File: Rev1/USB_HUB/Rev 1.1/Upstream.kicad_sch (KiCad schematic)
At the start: 17 parts, among them IC1 TLV76733DGNR, IC2 TLV76733DGNR, J4 F3311A7H121014E200, U7 USBLC6-2SC6, U8 USBLC6-2SC6

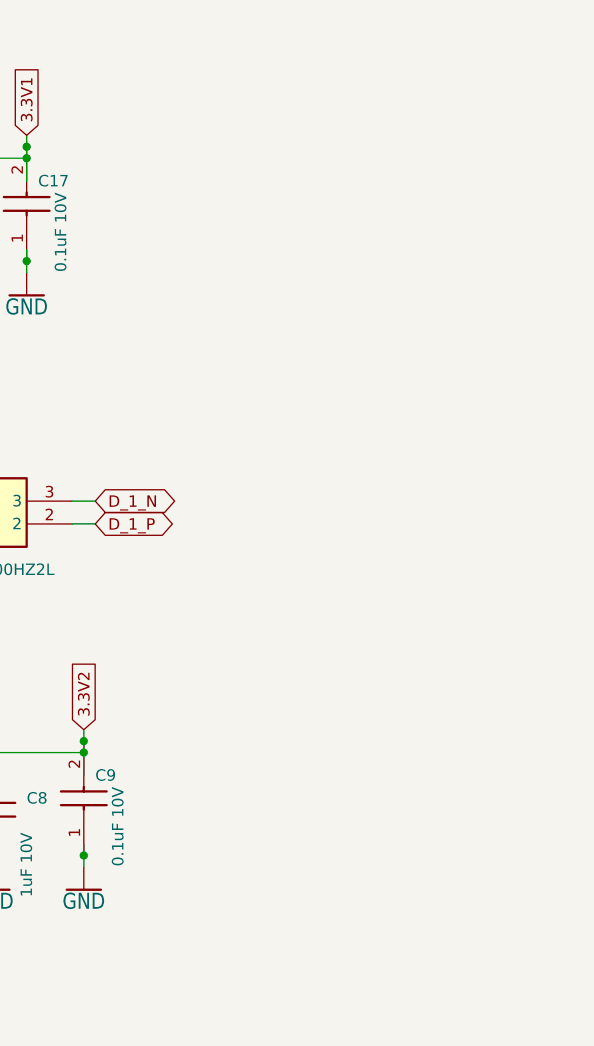
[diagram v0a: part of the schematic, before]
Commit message: Updated USB HUB Rev 1.1
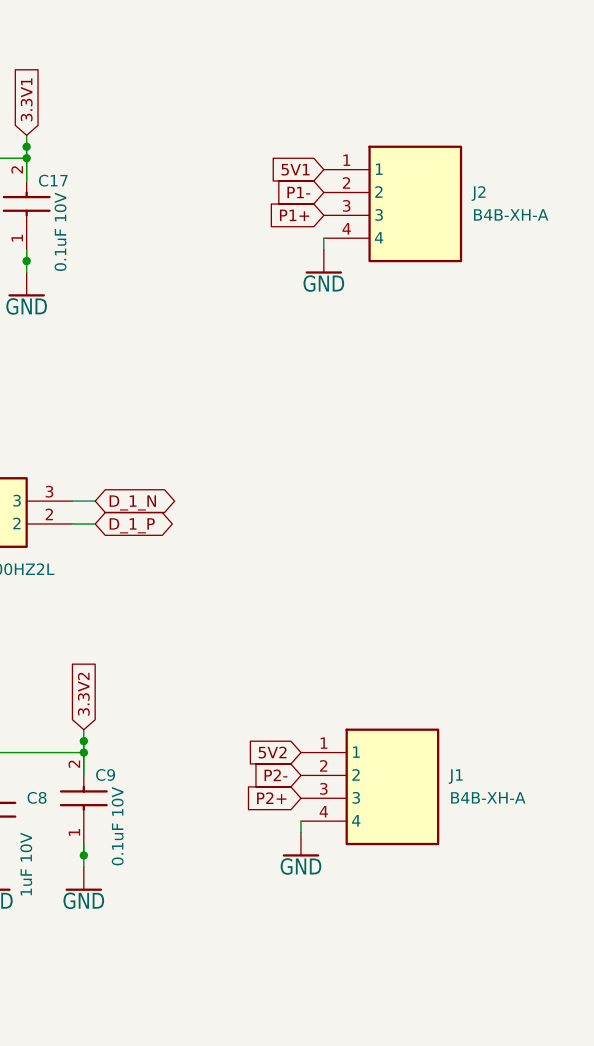
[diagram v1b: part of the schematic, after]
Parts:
- added J1, J2: B4B-XH-A, B4BXHA, symbol SamacSys_Parts:B4B-XH-A
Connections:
- net 5V1: now also J2.1
- net 5V2: now also J1.1
- net GND: now also J1.4, J2.4
- net P1+: now also J2.3
- net P1-: now also J2.2
- net P2+: now also J1.3
- net P2-: now also J1.2
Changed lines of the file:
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@@
+    (stroke (width 0.1524) (type solid))
+  )
+  (wire (pts (xy 245.11 127) (xy 245.11 125.73))
     (stroke (width 0.1524) (type solid))
   )
@@
   (wire (pts (xy 58.42 82.55) (xy 58.42 85.09))
     (stroke (width 0) (type default))
+  )
+  (wire (pts (xy 247.65 62.23) (xy 247.65 60.96))
+    (stroke (width 0.1524) (type solid))
   )
   (wire (pts (xy 214.63 63.5) (xy 214.63 62.23))
@@
     )
   )
+  (global_label "P1+" (shape input) (at 247.65 58.42 180) (fields_autoplaced)
+    (effects (font (size 1.27 1.27)) (justify right))
+    (property "Intersheetrefs" "${INTERSHEET_REFS}" (at 241.2671 58.42 0)
+      (effects (font (size 1.27 1.27)) (justify right) hide)
+    )
+  )
+  (global_label "P2-" (shape input) (at 245.11 120.65 180) (fields_autoplaced)
+    (effects (font (size 1.27 1.27)) (justify right))
+    (property "Intersheetrefs" "${INTERSHEET_REFS}" (at 238.7271 120.65 0)
+      (effects (font (size 1.27 1.27)) (justify right) hide)
+    )
+  )
   (global_label "D_N_2" (shape bidirectional) (at 222.25 158.75 0) (fields_autoplaced)
     (effects (font (size 1.27 1.27)) (justify left))
@@
     )
   )
+  (global_label "P1-" (shape input) (at 247.65 55.88 180) (fields_autoplaced)
+    (effects (font (size 1.27 1.27)) (justify right))
+    (property "Intersheetrefs" "${INTERSHEET_REFS}" (at 241.2671 55.88 0)
+      (effects (font (size 1.27 1.27)) (justify right) hide)
+    )
+  )
   (global_label "3.3V2" (shape input) (at 220.98 115.57 90) (fields_autoplaced)
     (effects (font (size 1.27 1.27)) (justify left))
@@
     )
   )
+  (global_label "5V1" (shape input) (at 247.65 53.34 180) (fields_autoplaced)
+    (effects (font (size 1.27 1.27)) (justify right))
+    (property "Intersheetrefs" "${INTERSHEET_REFS}" (at 241.8114 53.34 0)
+      (effects (font (size 1.27 1.27)) (justify right) hide)
+    )
+  )
+  (global_label "P2+" (shape input) (at 245.11 123.19 180) (fields_autoplaced)
+    (effects (font (size 1.27 1.27)) (justify right))
+    (property "Intersheetrefs" "${INTERSHEET_REFS}" (at 238.7271 123.19 0)
+      (effects (font (size 1.27 1.27)) (justify right) hide)
+    )
+  )
   (global_label "3.3V1" (shape input) (at 214.63 49.53 90) (fields_autoplaced)
     (effects (font (size 1.27 1.27)) (justify left))
@@
     )
   )
+  (global_label "5V2" (shape input) (at 245.11 118.11 180) (fields_autoplaced)
+    (effects (font (size 1.27 1.27)) (justify right))
+    (property "Intersheetrefs" "${INTERSHEET_REFS}" (at 239.2714 118.11 0)
+      (effects (font (size 1.27 1.27)) (justify right) hide)
+    )
+  )
   (global_label "5V2" (shape input) (at 154.94 156.21 0) (fields_autoplaced)
     (effects (font (size 1.27 1.27)) (justify left))
@@
     )
   )
+  (symbol (lib_id "SamacSys_Parts:B4B-XH-A") (at 245.11 118.11 0) (unit 1)
+    (in_bom yes) (on_board yes) (dnp no) (fields_autoplaced)
+    (property "Reference" "J1" (at 261.62 120.65 0)
+      (effects (font (size 1.27 1.27)) (justify left))
+    )
+    (property "Value" "B4B-XH-A" (at 261.62 123.19 0)
+      (effects (font (size 1.27 1.27)) (justify left))
+    )
+    (property "Footprint" "B4BXHA" (at 261.62 213.03 0)
+      (effects (font (size 1.27 1.27)) (justify left top) hide)
+    )
+    (property "Datasheet" "https://www.jst-mfg.com/product/pdf/eng/eXH.pdf" (at 261.62 313.03 0)
+      (effects (font (size 1.27 1.27)) (justify left top) hide)
+    )
+    (property "Height" "7" (at 261.62 513.03 0)
+      (effects (font (size 1.27 1.27)) (justify left top) hide)
+    )
+    (property "Manufacturer_Name" "JST (JAPAN SOLDERLESS TERMINALS)" (at 261.62 613.03 0)
+      (effects (font (size 1.27 1.27)) (justify left top) hide)
+    )
+    (property "Manufacturer_Part_Number" "B4B-XH-A" (at 261.62 713.03 0)
+      (effects (font (size 1.27 1.27)) (justify left top) hide)
+    )
+    (property "Mouser Part Number" "" (at 261.62 813.03 0)
+      (effects (font (size 1.27 1.27)) (justify left top) hide)
+    )
+    (property "Mouser Price/Stock" "" (at 261.62 913.03 0)
+      (effects (font (size 1.27 1.27)) (justify left top) hide)
+    )
+    (property "Arrow Part Number" "" (at 261.62 1013.03 0)
+      (effects (font (size 1.27 1.27)) (justify left top) hide)
+    )
+    (property "Arrow Price/Stock" "" (at 261.62 1113.03 0)
+      (effects (font (size 1.27 1.27)) (justify left top) hide)
+    )
+    (pin "3")
+    (pin "4")
+    (pin "2")
+    (pin "1")
+    (instances
+      (project "USB_Hub"
+        (path "/70f02035-c160-452a-9b74-4676c4cc3896/9d5d860f-6e3c-429f-a085-7a050f60d45d"
+          (reference "J1") (unit 1)
+        )
+      )
+    )
+  )
   (symbol (lib_id "Qwiic-USB_Hub-eagle-import:GND") (at 214.63 67.31 0) (unit 1)
     (in_bom yes) (on_board yes) (dnp no)
@@
         (path "/70f02035-c160-452a-9b74-4676c4cc3896/9d5d860f-6e3c-429f-a085-7a050f60d45d"
           (reference "#GND03") (unit 1)
+        )
+      )
+    )
+  )
+  (symbol (lib_id "Qwiic-USB_Hub-eagle-import:GND") (at 245.11 129.54 0) (unit 1)
+    (in_bom yes) (on_board yes) (dnp no)
+    (property "Reference" "#GND021" (at 245.11 129.54 0)
+      (effects (font (size 1.27 1.27)) hide)
+    )
+    (property "Value" "GND" (at 245.11 129.794 0)
+      (effects (font (size 1.778 1.5113)) (justify top))
+    )
+    (property "Footprint" "" (at 245.11 129.54 0)
+      (effects (font (size 1.27 1.27)) hide)
+    )
+    (property "Datasheet" "" (at 245.11 129.54 0)
+      (effects (font (size 1.27 1.27)) hide)
+    )
+    (pin "1")
+    (instances
+      (project "USB_Hub"
+        (path "/70f02035-c160-452a-9b74-4676c4cc3896/9d5d860f-6e3c-429f-a085-7a050f60d45d"
+          (reference "#GND021") (unit 1)
         )
       )
@@
         (path "/70f02035-c160-452a-9b74-4676c4cc3896/9d5d860f-6e3c-429f-a085-7a050f60d45d"
           (reference "FL1") (unit 1)
+        )
+      )
+    )
+  )
+  (symbol (lib_id "Qwiic-USB_Hub-eagle-import:GND") (at 247.65 64.77 0) (unit 1)
+    (in_bom yes) (on_board yes) (dnp no)
+    (property "Reference" "#GND022" (at 247.65 64.77 0)
+      (effects (font (size 1.27 1.27)) hide)
+    )
+    (property "Value" "GND" (at 247.65 65.024 0)
+      (effects (font (size 1.778 1.5113)) (justify top))
+    )
+    (property "Footprint" "" (at 247.65 64.77 0)
+      (effects (font (size 1.27 1.27)) hide)
+    )
+    (property "Datasheet" "" (at 247.65 64.77 0)
+      (effects (font (size 1.27 1.27)) hide)
+    )
+    (pin "1")
+    (instances
+      (project "USB_Hub"
+        (path "/70f02035-c160-452a-9b74-4676c4cc3896/9d5d860f-6e3c-429f-a085-7a050f60d45d"
+          (reference "#GND022") (unit 1)
         )
       )
@@
         )
       )
+    )
+  )
+  (symbol (lib_id "SamacSys_Parts:B4B-XH-A") (at 247.65 53.34 0) (unit 1)
+    (in_bom yes) (on_board yes) (dnp no) (fields_autoplaced)
+    (property "Reference" "J2" (at 264.16 55.88 0)
+      (effects (font (size 1.27 1.27)) (justify left))
+    )
+    (property "Value" "B4B-XH-A" (at 264.16 58.42 0)
+      (effects (font (size 1.27 1.27)) (justify left))
+    )
+    (property "Footprint" "B4BXHA" (at 264.16 148.26 0)
+      (effects (font (size 1.27 1.27)) (justify left top) hide)
+    )
+    (property "Datasheet" "https://www.jst-mfg.com/product/pdf/eng/eXH.pdf" (at 264.16 248.26 0)
+      (effects (font (size 1.27 1.27)) (justify left top) hide)
+    )
+    (property "Height" "7" (at 264.16 448.26 0)
+      (effects (font (size 1.27 1.27)) (justify left top) hide)
+    )
+    (property "Manufacturer_Name" "JST (JAPAN SOLDERLESS TERMINALS)" (at 264.16 548.26 0)
+      (effects (font (size 1.27 1.27)) (justify left top) hide)
+    )
+    (property "Manufacturer_Part_Number" "B4B-XH-A" (at 264.16 648.26 0)
+      (effects (font (size 1.27 1.27)) (justify left top) hide)
+    )
+    (property "Mouser Part Number" "" (at 264.16 748.26 0)
+      (effects (font (size 1.27 1.27)) (justify left top) hide)
+    )
+    (property "Mouser Price/Stock" "" (at 264.16 848.26 0)
+      (effects (font (size 1.27 1.27)) (justify left top) hide)
+    )
+    (property "Arrow Part Number" "" (at 264.16 948.26 0)
+      (effects (font (size 1.27 1.27)) (justify left top) hide)
+    )
+    (property "Arrow Price/Stock" "" (at 264.16 1048.26 0)
+      (effects (font (size 1.27 1.27)) (justify left top) hide)
+    )
+    (pin "3")
+    (pin "4")
+    (pin "2")
+    (pin "1")
+    (instances
+      (project "USB_Hub"
+        (path "/70f02035-c160-452a-9b74-4676c4cc3896/9d5d860f-6e3c-429f-a085-7a050f60d45d"
+          (reference "J2") (unit 1)
+        )
+      )
